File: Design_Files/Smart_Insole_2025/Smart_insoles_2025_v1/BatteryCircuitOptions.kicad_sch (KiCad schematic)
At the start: 10 parts, among them J3 S2B-PH-SM4-TB_LF__SN_, U5 BQ24040DSQR

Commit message: PCB new moving things around
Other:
- moved on the sheet: J3, TH1
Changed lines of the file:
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@@
 	)
 	(no_connect
-		(at 36.83 62.23)
+		(at 36.83 49.53)
 	)
 	(no_connect
-		(at 36.83 64.77)
+		(at 36.83 52.07)
 	)
 	(no_connect
@@
 	(wire
 		(pts
-			(xy 100.33 60.96) (xy 100.33 66.04)
+			(xy 104.14 59.69) (xy 104.14 62.23)
 		)
 		(stroke
@@
 	(wire
 		(pts
-			(xy 31.75 58.42) (xy 31.75 57.15)
+			(xy 31.75 45.72) (xy 31.75 44.45)
 		)
 		(stroke
@@
 	(wire
 		(pts
-			(xy 104.14 50.8) (xy 100.33 50.8)
-		)
-		(stroke
-			(width 0)
-			(type default)
-		)
-	)
-	(wire
-		(pts
 			(xy 153.67 38.1) (xy 143.51 38.1)
 		)
@@
 	(wire
 		(pts
-			(xy 100.33 44.45) (xy 95.25 44.45)
-		)
-		(stroke
-			(width 0)
-			(type default)
-		)
-	)
-	(wire
-		(pts
-			(xy 100.33 38.1) (xy 100.33 44.45)
+			(xy 101.6 44.45) (xy 95.25 44.45)
+		)
+		(stroke
+			(width 0)
+			(type default)
+		)
+	)
+	(wire
+		(pts
+			(xy 101.6 38.1) (xy 101.6 44.45)
 		)
 		(stroke
@@
 	(wire
 		(pts
-			(xy 31.75 57.15) (xy 36.83 57.15)
+			(xy 31.75 44.45) (xy 36.83 44.45)
 		)
 		(stroke
@@
 	(wire
 		(pts
-			(xy 100.33 50.8) (xy 100.33 53.34)
+			(xy 104.14 43.18) (xy 104.14 52.07)
 		)
 		(stroke
@@
 	(wire
 		(pts
-			(xy 104.14 38.1) (xy 100.33 38.1)
+			(xy 104.14 38.1) (xy 101.6 38.1)
 		)
 		(stroke
@@
 		(pts
 			(xy 104.14 35.56) (xy 95.25 35.56)
-		)
-		(stroke
-			(width 0)
-			(type default)
-		)
-	)
-	(wire
-		(pts
-			(xy 104.14 43.18) (xy 104.14 50.8)
 		)
 		(stroke
@@
 	(text "Jst Battery connector"
 		(exclude_from_sim no)
-		(at 48.514 49.784 0)
+		(at 48.514 37.084 0)
 		(effects
 			(font
@@
 	(symbol
 		(lib_id "power:+BATT")
-		(at 36.83 54.61 90)
+		(at 36.83 41.91 90)
 		(unit 1)
 		(exclude_from_sim no)
@@
 		(fields_autoplaced yes)
 		(property "Reference" "#PWR022"
-			(at 40.64 54.61 0)
+			(at 40.64 41.91 0)
 			(effects
 				(font
@@
 		)
 		(property "Value" "+BATT"
-			(at 33.655 54.61 90)
+			(at 33.655 41.91 90)
 			(effects
 				(font
@@
 		)
 		(property "Footprint" ""
-			(at 36.83 54.61 0)
+			(at 36.83 41.91 0)
 			(effects
 				(font
@@
 		)
 		(property "Datasheet" ""
-			(at 36.83 54.61 0)
+			(at 36.83 41.91 0)
 			(effects
 				(font
@@
 		)
 		(property "Description" "Power symbol creates a global label with name \"+BATT\""
-			(at 36.83 54.61 0)
+			(at 36.83 41.91 0)
 			(effects
 				(font
@@
 	(symbol
 		(lib_id "S2B-PH-SM4-TB_LF__SN_:S2B-PH-SM4-TB_LF__SN_")
-		(at 44.45 57.15 0)
+		(at 44.45 44.45 0)
 		(unit 1)
 		(exclude_from_sim no)
@@
 		(on_board yes)
 		(dnp no)
-		(fields_autoplaced yes)
 		(property "Reference" "J3"
-			(at 50.2412 58.4778 0)
+			(at 50.2412 45.7778 0)
 			(effects
 				(font
@@
 		)
 		(property "Value" "S2B-PH-SM4-TB_LF__SN_"
-			(at 50.2412 60.9021 0)
+			(at 32.004 56.896 0)
 			(effects
 				(font
@@
 		)
 		(property "Footprint" "JST-PH2-2.00MM-SMD-HORIZONTAL:JST_S2B-PH-SM4-TB_LF__SN_"
-			(at 44.45 57.15 0)
+			(at 44.45 44.45 0)
 			(effects
 				(font
@@
 		)
 		(property "Datasheet" ""
-			(at 44.45 57.15 0)
+			(at 44.45 44.45 0)
 			(effects
 				(font
@@
 		)
 		(property "Description" ""
-			(at 44.45 57.15 0)
+			(at 44.45 44.45 0)
 			(effects
 				(font
@@
 		)
 		(property "MF" "JST Sales"
-			(at 44.45 57.15 0)
+			(at 44.45 44.45 0)
 			(effects
 				(font
@@
 		)
 		(property "Description_1" "\n                        \n                            Connector Header Surface Mount, Right Angle 2 position 0.079 (2.00mm)\n                        \n"
-			(at 44.45 57.15 0)
+			(at 44.45 44.45 0)
 			(effects
 				(font
@@
 		)
 		(property "Package" "None"
-			(at 44.45 57.15 0)
+			(at 44.45 44.45 0)
 			(effects
 				(font
@@
 		)
 		(property "Price" "None"
-			(at 44.45 57.15 0)
+			(at 44.45 44.45 0)
 			(effects
 				(font
@@
 		)
 		(property "Check_prices" "https://www.snapeda.com/parts/S2B-PH-SM4-TB(LF)(SN)/JST/view-part/?ref=eda"
-			(at 44.45 57.15 0)
+			(at 44.45 44.45 0)
 			(effects
 				(font
@@
 		)
 		(property "STANDARD" "Manufacturer Recommendation"
-			(at 44.45 57.15 0)
+			(at 44.45 44.45 0)
 			(effects
 				(font
@@
 		)
 		(property "SnapEDA_Link" "https://www.snapeda.com/parts/S2B-PH-SM4-TB(LF)(SN)/JST/view-part/?ref=snap"
-			(at 44.45 57.15 0)
+			(at 44.45 44.45 0)
 			(effects
 				(font
@@
 		)
 		(property "MP" "S2B-PH-SM4-TB(LF)(SN)"
-			(at 44.45 57.15 0)
+			(at 44.45 44.45 0)
 			(effects
 				(font
@@
 		)
 		(property "Availability" "In Stock"
-			(at 44.45 57.15 0)
+			(at 44.45 44.45 0)
 			(effects
 				(font
@@
 		)
 		(property "MANUFACTURER" "JST"
-			(at 44.45 57.15 0)
+			(at 44.45 44.45 0)
 			(effects
 				(font
@@
 	(symbol
 		(lib_id "power:GND")
-		(at 31.75 58.42 0)
+		(at 31.75 45.72 0)
 		(unit 1)
 		(exclude_from_sim no)
@@
 		(fields_autoplaced yes)
 		(property "Reference" "#PWR023"
-			(at 31.75 64.77 0)
+			(at 31.75 52.07 0)
 			(effects
 				(font
@@
 		)
 		(property "Value" "GND"
-			(at 31.75 62.5531 0)
+			(at 31.75 49.8531 0)
 			(effects
 				(font
@@
 		)
 		(property "Footprint" ""
-			(at 31.75 58.42 0)
+			(at 31.75 45.72 0)
 			(effects
 				(font
@@
 		)
 		(property "Datasheet" ""
-			(at 31.75 58.42 0)
+			(at 31.75 45.72 0)
 			(effects
 				(font
@@
 		)
 		(property "Description" "Power symbol creates a global label with name \"GND\" , ground"
-			(at 31.75 58.42 0)
+			(at 31.75 45.72 0)
 			(effects
 				(font
@@
 	(symbol
 		(lib_id "power:GND")
-		(at 100.33 66.04 0)
+		(at 104.14 62.23 0)
 		(unit 1)
 		(exclude_from_sim no)
@@
 		(fields_autoplaced yes)
 		(property "Reference" "#PWR047"
-			(at 100.33 72.39 0)
+			(at 104.14 68.58 0)
 			(effects
 				(font
@@
 		)
 		(property "Value" "GND"
-			(at 100.33 70.1731 0)
+			(at 104.14 66.3631 0)
 			(effects
 				(font
@@
 		)
 		(property "Footprint" ""
-			(at 100.33 66.04 0)
+			(at 104.14 62.23 0)
 			(effects
 				(font
@@
 		)
 		(property "Datasheet" ""
-			(at 100.33 66.04 0)
+			(at 104.14 62.23 0)
 			(effects
 				(font
@@
 		)
 		(property "Description" "Power symbol creates a global label with name \"GND\" , ground"
-			(at 100.33 66.04 0)
+			(at 104.14 62.23 0)
 			(effects
 				(font
@@
 	(symbol
 		(lib_id "Device:Thermistor_NTC")
-		(at 100.33 57.15 0)
+		(at 104.14 55.88 0)
 		(unit 1)
 		(exclude_from_sim no)
@@
 		(fields_autoplaced yes)
 		(property "Reference" "TH1"
-			(at 102.743 56.2553 0)
+			(at 106.553 54.9853 0)
 			(effects
 				(font
@@
 		)
 		(property "Value" "Thermistor_NTC"
-			(at 102.743 58.6796 0)
+			(at 106.553 57.4096 0)
 			(effects
 				(font
@@
 		)
 		(property "Footprint" ""
-			(at 100.33 55.88 0)
+			(at 104.14 54.61 0)
 			(effects
 				(font
@@
 		)
 		(property "Datasheet" "~"
-			(at 100.33 55.88 0)
+			(at 104.14 54.61 0)
 			(effects
 				(font
@@
 		)
 		(property "Description" "Temperature dependent resistor, negative temperature coefficient"
-			(at 100.33 57.15 0)
+			(at 104.14 55.88 0)
 			(effects
 				(font
@@
 		)
 		(instances
-			(project ""
+			(project "Smart_insoles_2025_v1"
 				(path "/f1f3d712-154d-4111-a7c4-f47541abccf8/720d2e8f-49b8-46ab-8d82-07d24ffc5c73"
 					(reference "TH1")

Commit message: Changed Mcu to esp32c3 mini 1 n4
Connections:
- net 5V_IN renamed VBUS
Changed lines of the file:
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@@
-	)
-	(junction
-		(at 85.09 33.02)
-		(diameter 0)
-		(color 0 0 0 0)
 	)
 	(junction
@@
 	(wire
 		(pts
+			(xy 173.99 38.1) (xy 163.83 38.1)
+		)
+		(stroke
+			(width 0)
+			(type default)
+		)
+	)
+	(wire
+		(pts
 			(xy 153.67 38.1) (xy 143.51 38.1)
 		)
@@
 		(pts
 			(xy 143.51 50.8) (xy 143.51 53.34)
-		)
-		(stroke
-			(width 0)
-			(type default)
-		)
-	)
-	(wire
-		(pts
-			(xy 85.09 31.75) (xy 85.09 33.02)
 		)
 		(stroke
@@
 	(rectangle
 		(start 24.13 19.05)
-		(end 185.42 107.95)
+		(end 209.55 107.95)
 		(stroke
 			(width 0)
@@
 		)
 	)
-	(label "5V_IN"
-		(at 85.09 31.75 0)
-		(fields_autoplaced yes)
+	(global_label "VBUS"
+		(shape input)
+		(at 85.09 33.02 180)
 		(effects
 			(font
 				(size 1.27 1.27)
 			)
-			(justify left bottom)
+			(justify right)
+		)
+		(property "Intersheetrefs" "${INTERSHEET_REFS}"
+			(at 85.09 33.02 0)
+			(effects
+				(font
+					(size 1.27 1.27)
+				)
+				(hide yes)
+			)
 		)
 	)
@@
 	(symbol
 		(lib_id "power:+BATT")
-		(at 163.83 38.1 270)
+		(at 173.99 38.1 270)
 		(unit 1)
 		(exclude_from_sim no)
@@
 		(fields_autoplaced yes)
 		(property "Reference" "#PWR042"
-			(at 160.02 38.1 0)
+			(at 170.18 38.1 0)
 			(effects
 				(font
@@
 		)
 		(property "Value" "+BATT"
-			(at 167.005 38.1 90)
+			(at 177.165 38.1 90)
 			(effects
 				(font
@@
 		)
 		(property "Footprint" ""
-			(at 163.83 38.1 0)
+			(at 173.99 38.1 0)
 			(effects
 				(font
@@
 		)
 		(property "Datasheet" ""
-			(at 163.83 38.1 0)
+			(at 173.99 38.1 0)
 			(effects
 				(font
@@
 		)
 		(property "Description" "Power symbol creates a global label with name \"+BATT\""
-			(at 163.83 38.1 0)
-			(effects
-				(font
+			(at 173.99 38.1 0)
+			(effects
+				(font

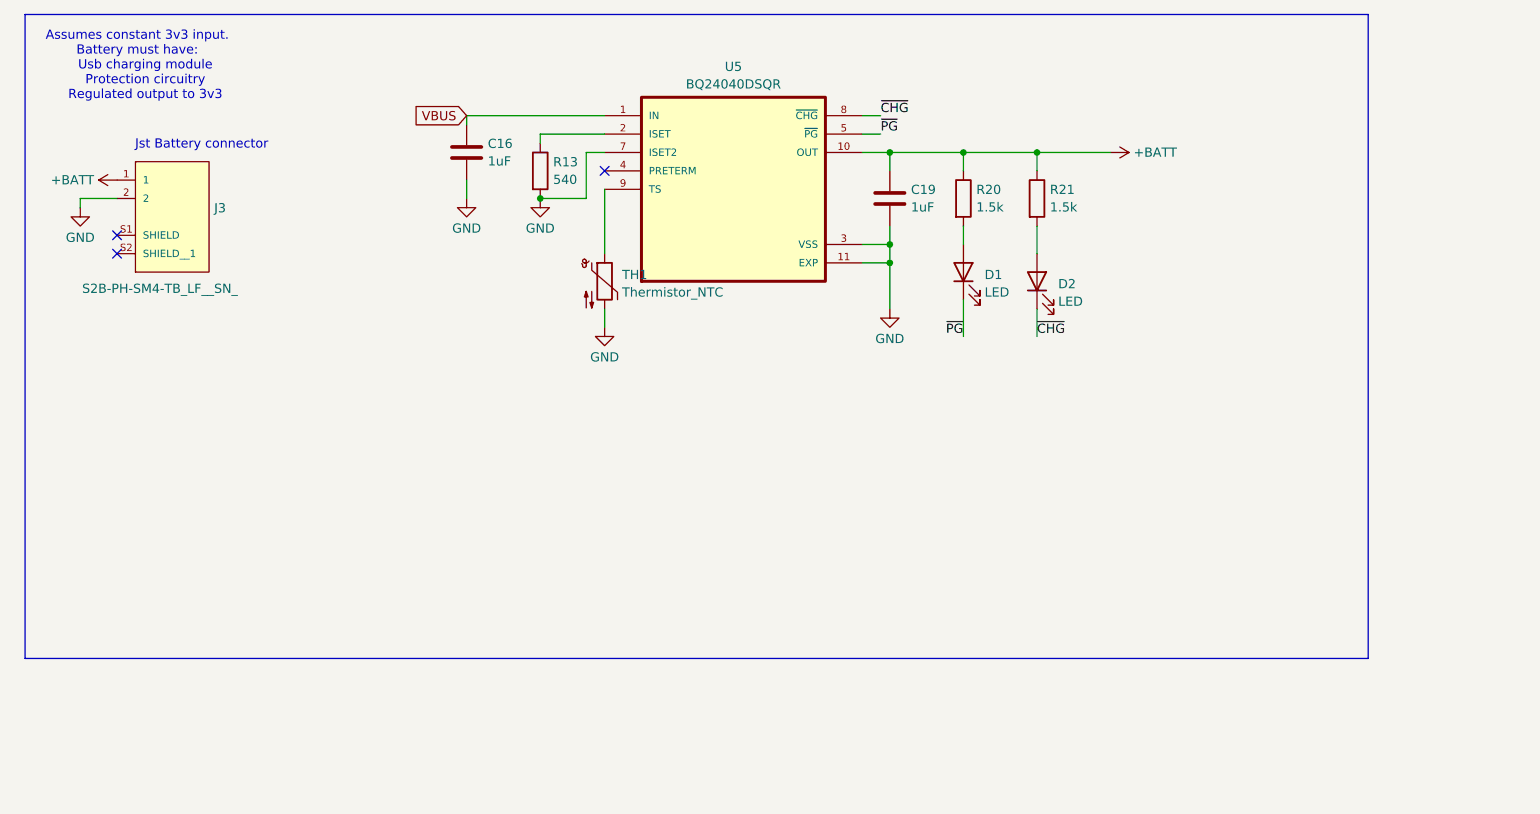
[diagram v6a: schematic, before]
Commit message: SCH: Advances in Battery circuit. Added External_Periph sheet
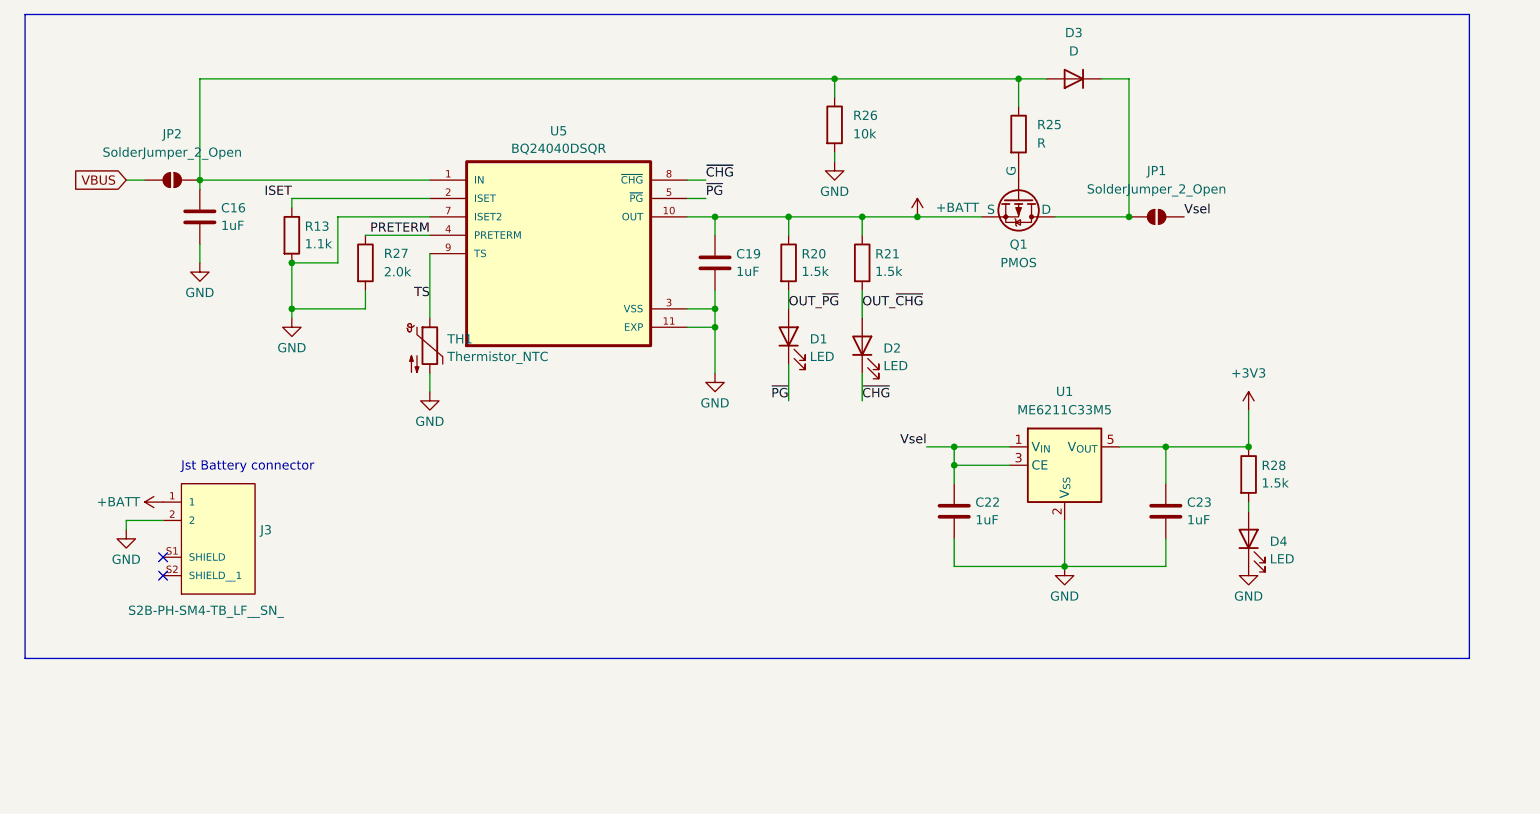
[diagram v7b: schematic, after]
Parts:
- added C22, C23: 1uF, Capacitor_SMD:C_0603_1608Metric, symbol Device:C
- added D3: D, symbol Device:D
- added D4: LED, LED_SMD:LED_0603_1608Metric, symbol Device:LED
- added JP1, JP2: SolderJumper_2_Open, symbol Jumper:SolderJumper_2_Open
- added Q1: PMOS, symbol Simulation_SPICE:PMOS
- added R25: R, symbol Device:R
- added R26: 10k, symbol Device:R
- added R27: 2.0k, Resistor_SMD:R_0603_1608Metric, symbol Device:R
- added R28: 1.5k, Resistor_SMD:R_0603_1608Metric, symbol Device:R
- added U1: ME6211C33M5, Package_TO_SOT_SMD:SOT-23-5, symbol Regulator_Linear:ME6211C33M5
- R13: value 540 -> 1.1k
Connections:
- net +BATT: now also Q1.3 (S)
- net GND: now also C22.1, C23.1, D4.1 (K), R26.2, R27.2, U1.2 (V_{SS})
- net VBUS: now also JP2.1 (A); no longer C16.2, U5.1 (IN)
- net ISET: now reaches R13.1, U5.2 (ISET)
- net OUT_~{PG}: now reaches D1.2 (A), R20.2
- net OUT_~{CHG}: now reaches D2.2 (A), R21.2
- net TS: now reaches TH1.1, U5.9 (TS)
- net PRETERM: now reaches U5.4 (PRETERM)
- net PRETERM: now also R27.1
- new net: D3.1 (K), JP1.1 (A), Q1.1 (D)
- new net: Q1.2 (G), R25.2
- new net: C16.2, D3.2 (A), JP2.2 (B), R25.1, R26.1, U5.1 (IN)
- new net: D4.2 (A), R28.2
- new net +3V3: C23.2, R28.1, U1.5 (V_{OUT})
- new net Vsel: C22.2, JP1.2 (B), U1.1 (V_{IN}), U1.3 (CE)
- no-connect marks 3 -> 2
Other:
- note removed: "Assumes constant 3v3 input. Battery must have: Usb charging module Protection circuitry Regulated output to 3v3"
- moved on the sheet: C16, C19, D1, D2, J3, R13, R20, R21, TH1, U5

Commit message: SCH: Added TVS diode on USB. Defined transistor and diode for battery/usb charging/switching
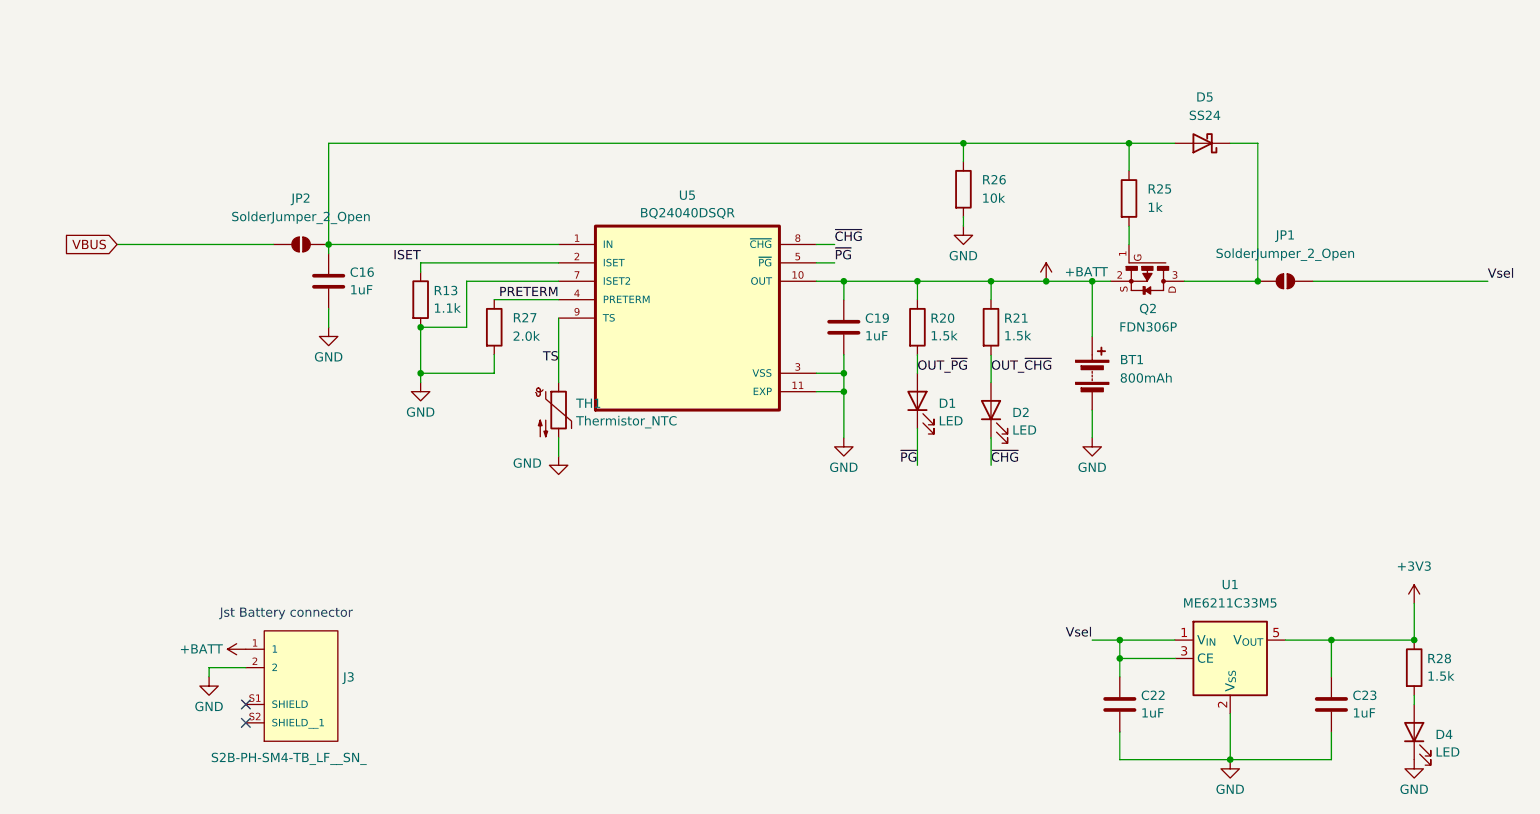
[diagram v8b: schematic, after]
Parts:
- removed D3: D, symbol Device:D
- removed Q1: PMOS, symbol Simulation_SPICE:PMOS
- added BT1: 800mAh, symbol Device:Battery
- added D5: SS24, Diode_SMD:D_SMA, symbol Diode:SS24
- added Q2: FDN306P, FDN306P:SSOT-3, symbol FDN306P:FDN306P
- R25: value R -> 1k
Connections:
- net +BATT: now also BT1.1 (+), Q2.2
- net GND: now also BT1.2 (-)
- net at JP1.1 (A): now also D5.1 (K), Q2.3
- net at R25.2: now also Q2.1
- net at C16.2, JP2.2 (B), R25.1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: now also D5.2 (A)
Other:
- moved on the sheet: C16, C19, C22, C23, D1, D2, D4, J3, JP1, JP2, R13, R20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
